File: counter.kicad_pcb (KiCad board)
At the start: 2 copper layers, 130.2 x 54 mm, 64 parts, among them J1 Barrel_Jack, SW1 Reset, SW2 Stop, SW3 Start, U1 SG531P, U2 4017, U3 SN74LS74, U5 4060, U6 NE555, U7 LM7805MPX_NOPB

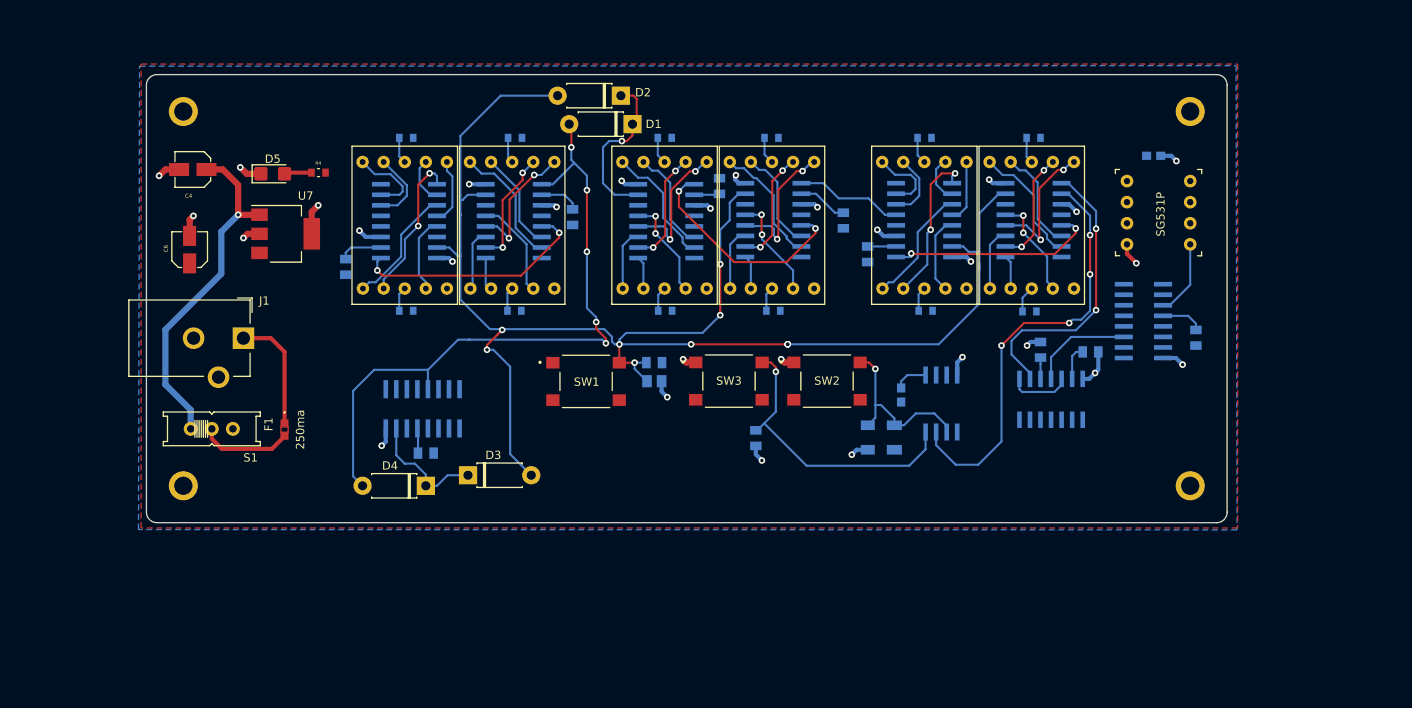
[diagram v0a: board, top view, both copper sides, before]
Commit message: Cleaned up schematic and pcb. Created annotations.
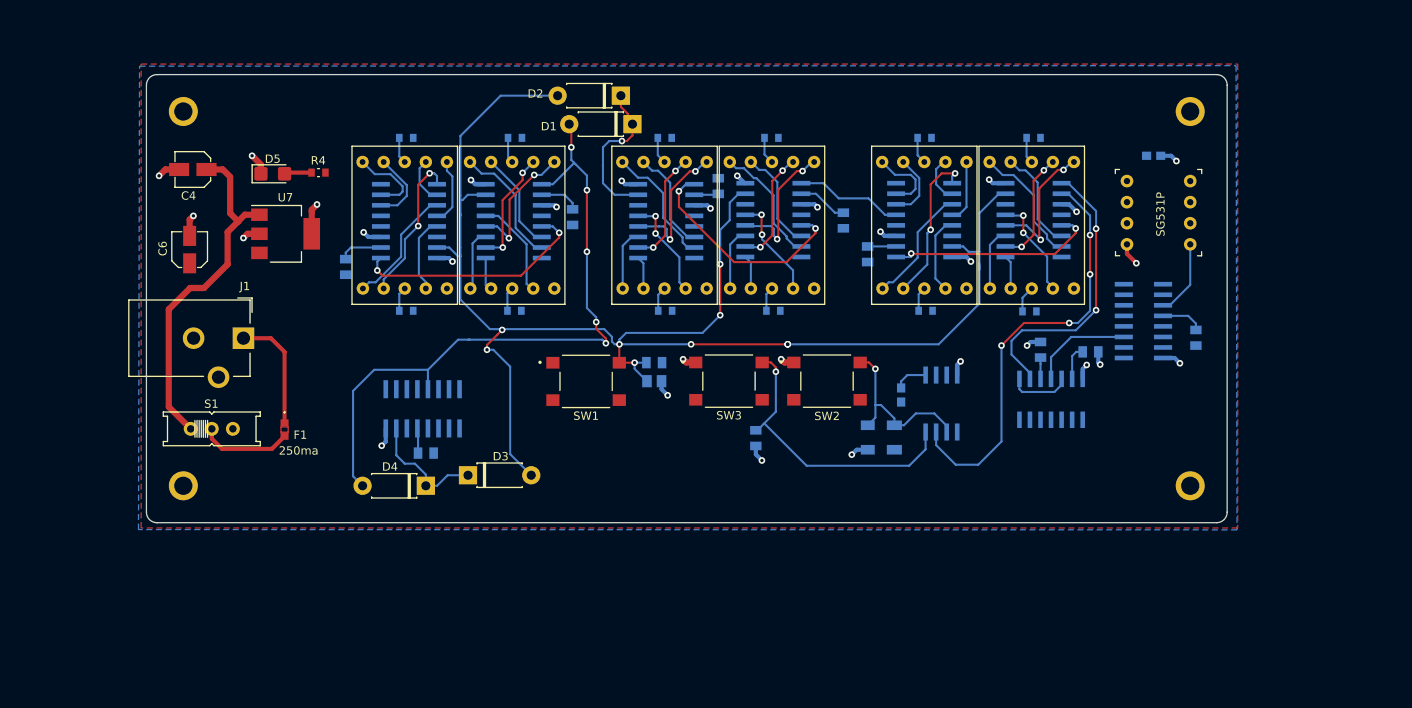
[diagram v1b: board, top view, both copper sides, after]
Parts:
- moved R14 0.14 mm to (131.7, 80.1)
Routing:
- net +5V: track 49.1 -> 44.9 mm, vias 21 -> 22
- net Net-(D1-Pad1): track 20.2 -> 18.8 mm
- net Net-(C4-Pad1): track 41.4 -> 42.4 mm, vias 1 -> 0

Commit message: Changed layout, organized traces, removed resistors from 7-seg displays
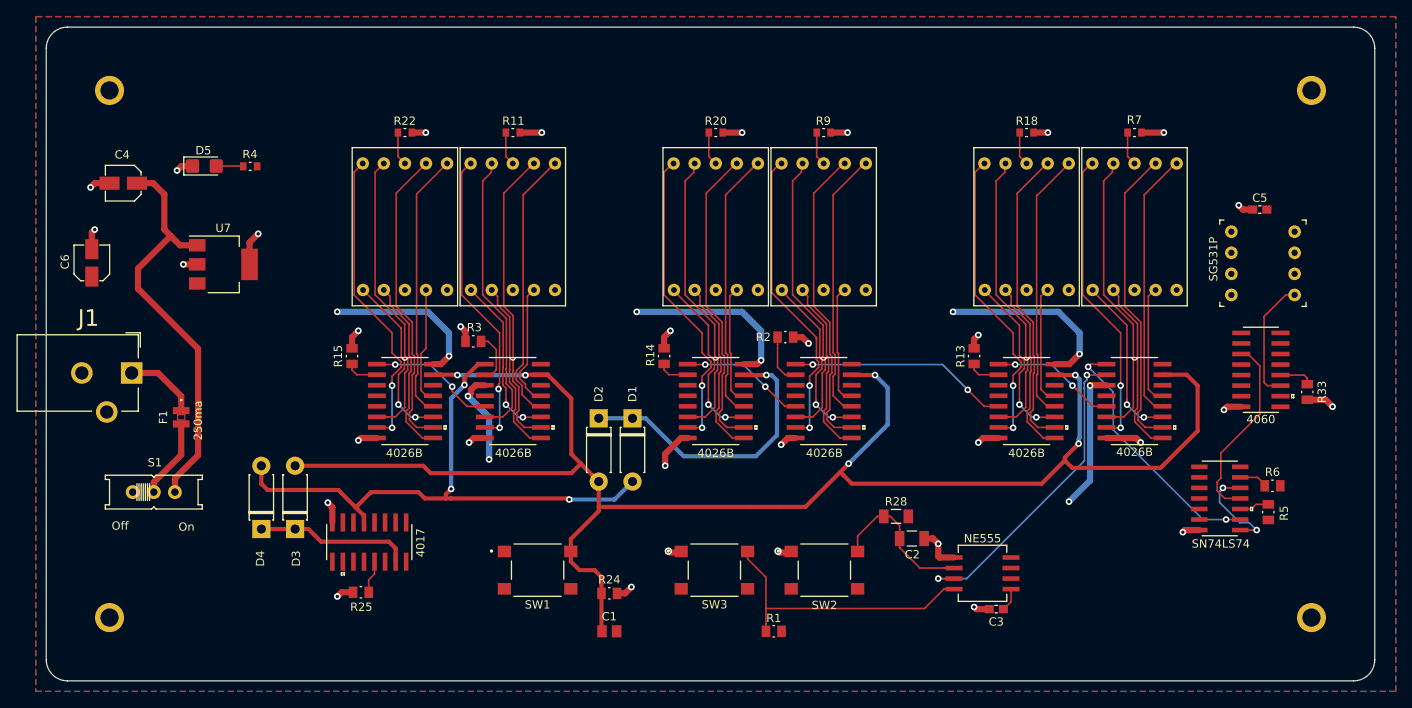
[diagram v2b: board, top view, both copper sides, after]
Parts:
- removed R10, R12, R19, R21, R23, R8: 120, footprints:RESC1608X55N
- removed REF** (x2): MountingHole_2.2mm_M2_ISO7380_Pad, MountingHole:MountingHole_2.2mm_M2_ISO7380_Pad
- added M2: MountingHole_2.2mm_M2_ISO7380_Pad, MountingHole:MountingHole_2.2mm_M2_ISO7380_Pad, F.Cu at (203.2, 68.6)
- added M2: MountingHole_2.2mm_M2_ISO7380_Pad, MountingHole:MountingHole_2.2mm_M2_ISO7380_Pad, F.Cu at (58.4, 68.6)
- C1, C2, C3, C5, R1, R11, R13, R14, R15, R18, R2, R20, R22, R24, R25, R28, R3, R33, R5, R6, R7, R9, U2, U3, U5, U6, milli1, milli2, min1, min2, sec1, sec2: moved to F.Cu
- moved D2 39.0 mm to (117.3, 108.1), turned to 270 degrees
- moved D1 35.4 mm to (121.4, 108.1), turned to 270 degrees
- moved R5 33.7 mm to (198.0, 119.4), turned to 90 degrees
- moved C1 30.6 mm to (118.6, 133.7)
- moved R24 28.3 mm to (118.6, 129.2)
- moved C3 28.2 mm to (165.2, 131.1), turned to 180 degrees
- moved R6 27.2 mm to (198.5, 116.2)
- moved milli2 25.1 mm to (168.9, 106.0)
- moved milli1 25.0 mm to (181.9, 106.0), turned to 0 degrees
- moved U3 23.6 mm to (192.2, 117.7), turned to 0 degrees
- moved SW1 23.5 mm to (110.0, 126.4)
- moved R1 23.4 mm to (138.4, 133.7), turned to 180 degrees
- moved M2 23.4 mm to (205.7, 132.1)
- moved SW3 22.8 mm to (131.3, 126.4)
- moved SW2 22.8 mm to (144.5, 126.4)
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- renumbered REF** to M2
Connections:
- S1 pad O: Net-(C4-Pad1) -> Net-(S1-PadO)
- S1 pad S: Net-(S1-PadS) -> Net-(C4-Pad1)
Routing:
- net GND: track 20.0 -> 82.3 mm, vias 8 -> 33
- net +5V: track 44.9 -> 92.2 mm, vias 22 -> 10
- net Net-(7seg_milli2-Pad7): track 5.29 -> 36.6 mm
- net Net-(7seg_min2-Pad7): track 5.60 -> 36.7 mm
- net Net-(7seg_milli2-Pad10): track 8.62 -> 36.8 mm, vias 0 -> 2
- net Net-(7seg_min2-Pad10): track 9.46 -> 36.9 mm, vias 0 -> 2
- net Net-(7seg_milli2-Pad9): track 8.09 -> 35.3 mm
- net Net-(7seg_min2-Pad9): track 8.83 -> 35.4 mm
- net Net-(7seg_milli2-Pad6): track 7.55 -> 32.3 mm
- net Net-(7seg_min2-Pad6): track 8.00 -> 32.3 mm
- net Net-(7seg_min1-Pad9): track 12.0 -> 35.1 mm
- net Net-(7seg_sec2-Pad9): track 12.5 -> 35.4 mm
- net Net-(7seg_sec1-Pad9): track 12.5 -> 35.4 mm
- net Net-(7seg_sec1-Pad7): track 13.8 -> 36.7 mm, vias 2 -> 0
- net Net-(7seg_sec2-Pad7): track 13.8 -> 36.7 mm, vias 2 -> 0
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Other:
- board size 130.2 x 54 mm -> 160 x 78.7 mm
- board text added: "Off"
- board text added: "On"

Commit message: added gerbers, footprints, schematic pdf, symbols, 3d models
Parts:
- removed M2: MountingHole_2.2mm_M2_ISO7380_Pad, MountingHole:MountingHole_2.2mm_M2_ISO7380_Pad
- added m2: MountingHole_2.2mm_M2_ISO7380_Pad, MountingHole:MountingHole_2.2mm_M2_ISO7380_Pad, F.Cu at (203.2, 69.8)
- moved C6 20.8 mm to (75.4, 97.6), turned to 0 degrees
- moved R4 1.66 mm to (73.9, 78.5), turned to 270 degrees
- moved m2 1.27 mm to (205.7, 130.8)
- moved m2 1.27 mm to (55.2, 133.3)
- moved m2 1.27 mm to (58.4, 69.8)
- moved R28 0.57 mm to (153.3, 119.3)
- moved F1 0.05 mm to (67.1, 108.0)
- renumbered M2 to m2
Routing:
- net +5V: track 92.2 -> 609.0 mm, vias 10 -> 12
- net 100Hz: track 30.9 -> 36.9 mm
- net Reset: track 205.9 -> 209.3 mm
- net Modulo6: track 70.9 -> 74.1 mm
- net GND: track 82.3 -> 80.7 mm
- net Stop: track 18.6 -> 20.2 mm
- net Net-(U3-Pad12): track 11.8 -> 10.4 mm
- net Net-(C4-Pad1): track 49.5 -> 50.8 mm
- net Start: track 34.2 -> 34.9 mm
- net Net-(D5-Pad2): track 3.27 -> 2.64 mm
- net Net-(D1-Pad1): track 35.3 -> 34.8 mm
- removed copper zone on F.Cu, net +5V
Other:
- board size 160 x 78.7 mm -> 160 x 75.7 mm
- net class Default: clearance 0.2 -> 0.15
- rule solder_mask_min_width: 0.25 -> 0.15
- rule trace_clearance: 0.2 -> 0.15
- board text added: "+"
- board text added: "-"

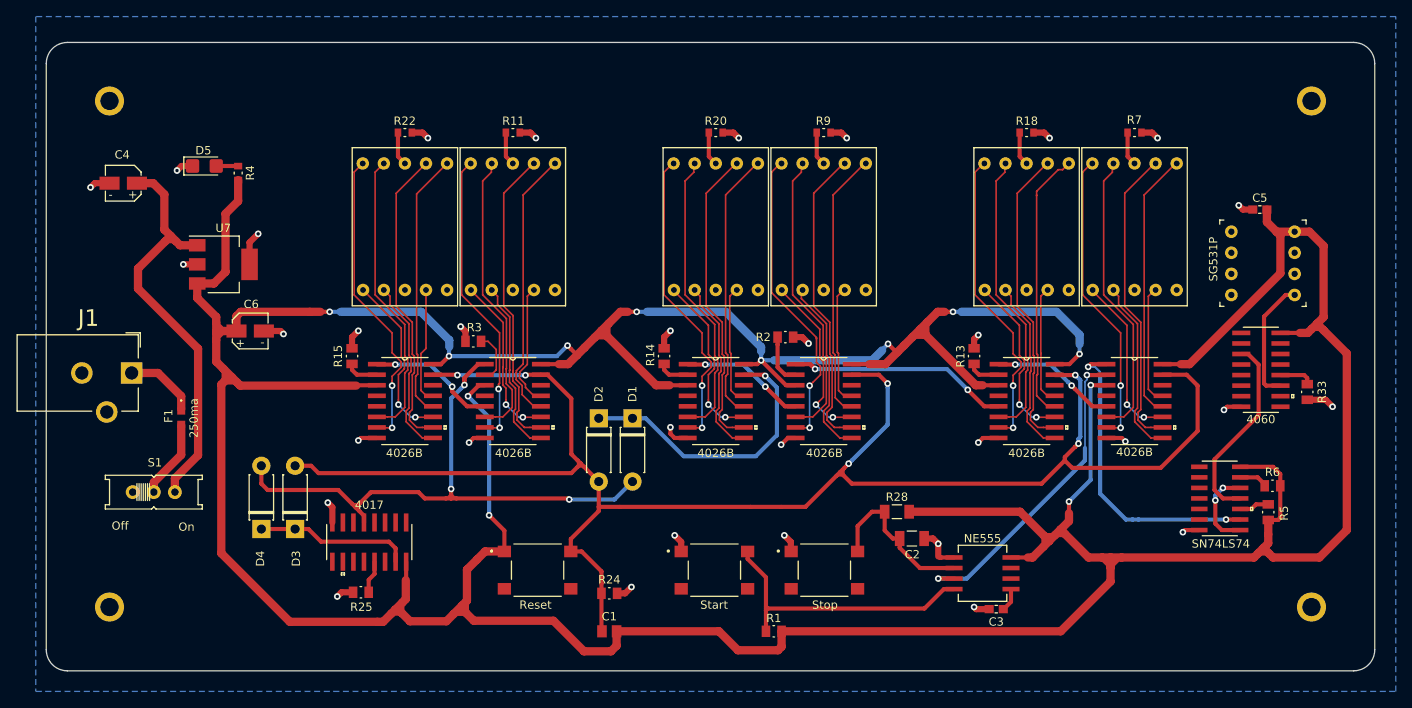
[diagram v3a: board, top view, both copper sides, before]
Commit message: Rev 2 board. Added missing trace, gerbers, and schematic
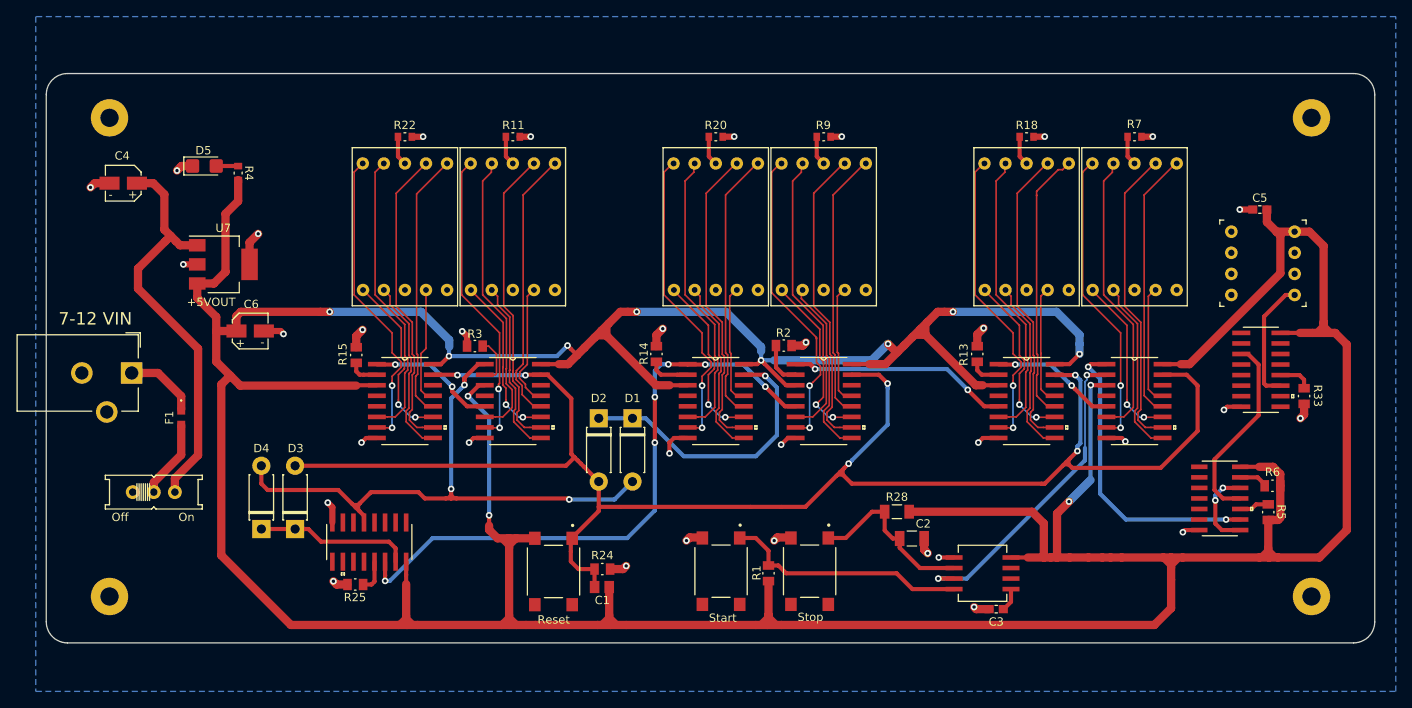
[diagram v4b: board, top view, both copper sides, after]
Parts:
- F1: value 250ma -> 375ma
- SW1: value Reset -> Stop
- SW2: value Stop -> Start
- SW3: value Start -> Reset
- moved SW1 32.8 mm to (142.7, 126.5), turned to 270 degrees
- moved SW3 19.4 mm to (111.9, 126.5), turned to 270 degrees
- moved SW2 12.4 mm to (132.1, 126.5), turned to 270 degrees
- moved R1 7.01 mm to (137.8, 126.7), turned to 90 degrees
- moved C1 5.41 mm to (117.7, 128.4)
- moved R24 3.04 mm to (117.8, 126.2)
- moved m2 2.03 mm to (203.2, 71.9)
- moved m2 2.03 mm to (58.4, 71.9)
- moved m2 1.27 mm to (205.7, 129.5)
- moved m2 1.27 mm to (55.2, 132.1)
- moved R25 1.15 mm to (88.0, 128.1)
- moved R2 1.03 mm to (139.6, 99.3)
- moved R14 0.96 mm to (124.3, 100.3)
- moved R33 0.63 mm to (202.3, 105.4)
- moved R3 0.60 mm to (102.4, 99.4)
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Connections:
- SW1 pad 1: +5V -> Stop
- SW1 pad 2: Reset -> Net-(SW1-Pad2)
- SW1 pad 3: (no net) -> GND
- SW1 pad 4: (no net) -> Net-(SW1-Pad4)
- SW2 pad 1: GND -> Start
- SW2 pad 2: Stop -> Net-(SW2-Pad2)
- SW2 pad 3: (no net) -> GND
- SW2 pad 4: (no net) -> Net-(SW2-Pad4)
- SW3 pad 1: GND -> Reset
- SW3 pad 2: Start -> Net-(SW3-Pad2)
- SW3 pad 3: (no net) -> +5V
- SW3 pad 4: (no net) -> Net-(SW3-Pad4)
- U2 pad 14: sec1_carry -> carry_sec1
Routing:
- net carry_sec1: track 15.1 -> 74.6 mm, vias 2 -> 6
- net +5V: track 609.0 -> 634.0 mm
- net GND: track 80.7 -> 71.7 mm, vias 33 -> 34
- net Reset: track 209.3 -> 202.6 mm
- net Start: track 34.9 -> 29.5 mm
- net Net-(C4-Pad1): track 50.8 -> 49.5 mm
- net Net-(R14-Pad1): track 3.80 -> 5.01 mm
- net Stop: track 20.2 -> 21.2 mm
- net Net-(R2-Pad1): track 6.18 -> 5.35 mm
- net Net-(7seg_sec2-Pad8): track 4.07 -> 3.56 mm
- net Net-(7seg_sec1-Pad8): track 4.07 -> 3.56 mm
- net Net-(7seg_min2-Pad8): track 4.07 -> 3.56 mm
- net Net-(7seg_min1-Pad8): track 4.07 -> 3.56 mm
- net Net-(7seg_milli2-Pad8): track 4.07 -> 3.56 mm
- net Net-(7seg_milli1-Pad8): track 4.07 -> 3.56 mm
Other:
- board size 160 x 75.7 mm -> 160 x 68.6 mm
- board text added: "+5VOUT"
- board text added: "4017"
- board text added: "7-12 VIN"
- board text added: "Reset"
- board text added: "Start"
- board text added: "Stop"

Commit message: initial commit
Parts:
- removed F1: 375ma, footprints:F0603E0R25FSTR
- C4, C6: footprint footprints:CAPAE430X550N -> counter:CAPAE430X550N
- C5: footprint footprints:CAPC1608X90 -> counter:CAPC1608X90
- R4: footprint footprints:RESC1608X55N -> counter:RESC1608X55N
- S1: footprint EG1218 -> counter:EG1218
- SW1, SW2, SW3: footprint footprints:SW_B3FS-1010P -> counter:SW_B3FS-1010P
- moved R1 20.3 mm to (157.8, 130.0), turned to 270 degrees
- moved R28 9.65 mm to (162.9, 120.0)
- moved C2 7.82 mm to (162.9, 122.1)
- moved R14 4.98 mm to (125.7, 105.1), turned to 270 degrees
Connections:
- J1 pad 1: Net-(F1-Pad1) -> /+7-12VIN
- S1 pad P: Net-(F1-Pad2) -> /+7-12VIN
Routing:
- net +5V: track 634.0 -> 89.5 mm
- net Net-(C4-Pad1): track 49.5 -> 0.00 mm
- net GND: track 71.7 -> 47.0 mm, vias 34 -> 35
- net Net-(F1-Pad2): track 9.42 -> 0.00 mm
- net Net-(F1-Pad1): track 8.70 -> 0.00 mm
- net Net-(D1-Pad1): track 34.8 -> 29.6 mm
- net Stop: track 21.2 -> 25.7 mm
- net Start: track 29.5 -> 31.4 mm
- net Net-(R14-Pad1): track 5.01 -> 3.25 mm
- added copper zone on F.Cu, net +5V
- added copper zone on F.Cu, net /+7-12VIN
- added copper zone on F.Cu, net GND
- added copper zone on F.Cu, net Net-(C4-Pad1)
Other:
- board text added: "COUNTER_V01"
